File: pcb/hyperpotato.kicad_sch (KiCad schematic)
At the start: 61 parts, among them J1 Conn_01x05, J2 Conn_01x02_Socket, J3 Conn_01x04, J4 Conn_01x04, J5 Conn_01x04, J6 Conn_01x05, K1 SW_Push, K10 SW_Push, K11 SW_Push, K12 SW_Push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

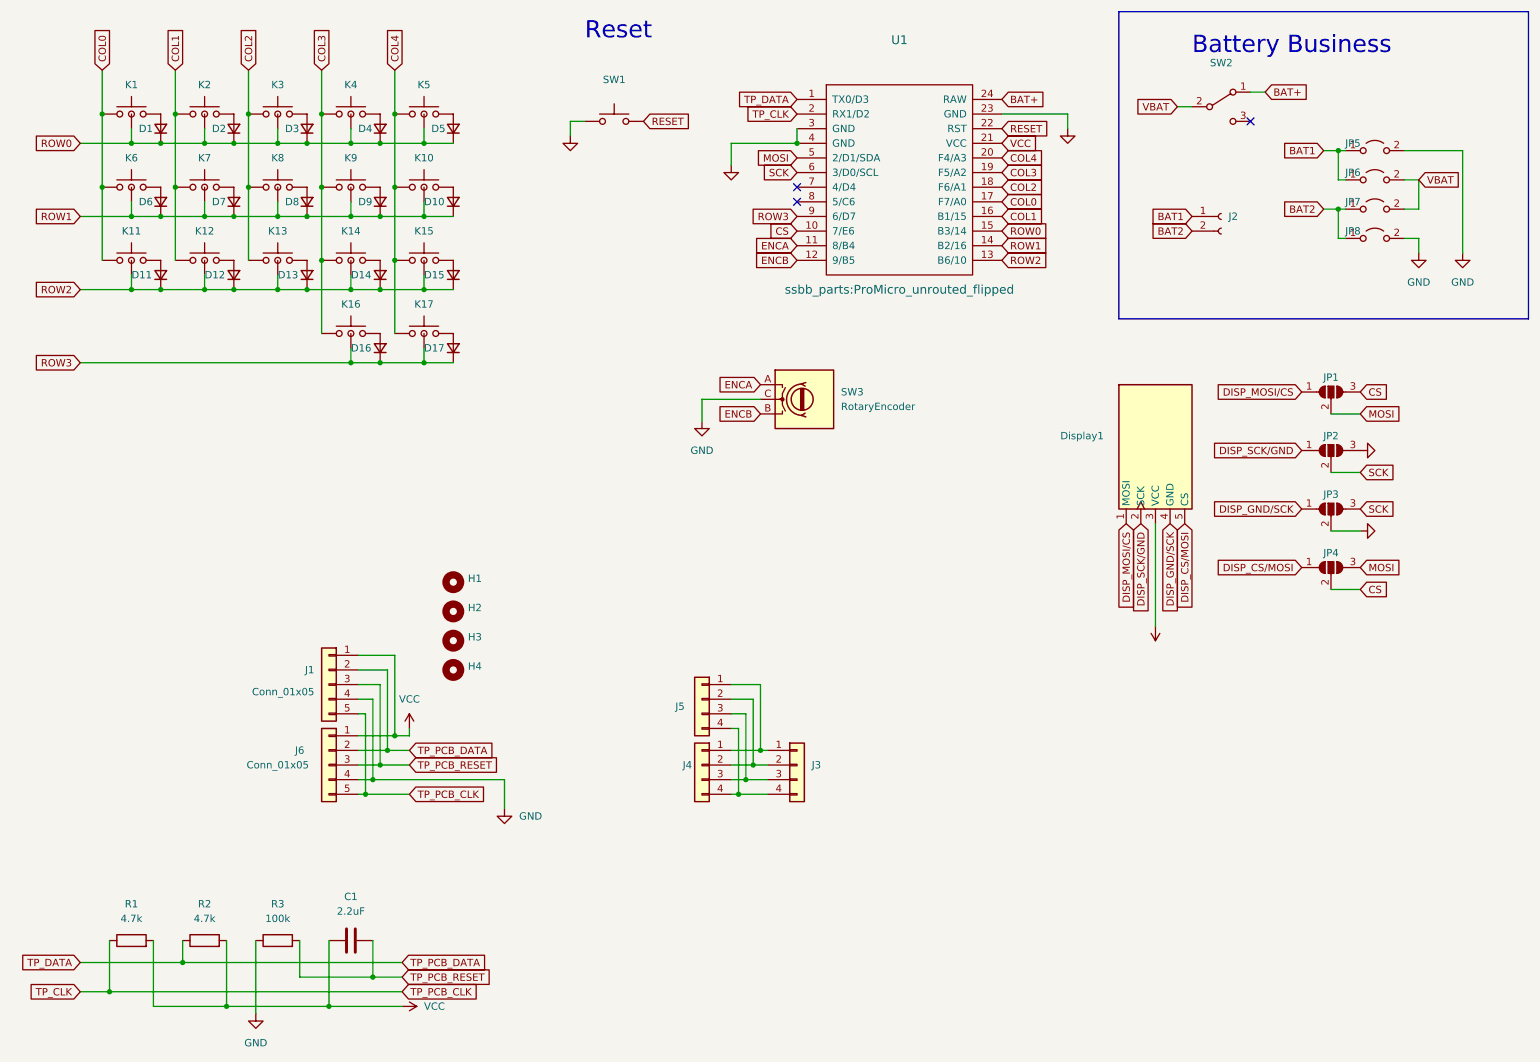
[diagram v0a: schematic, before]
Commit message: Revert "Prepare rev1.3"
This reverts commit 189d012c5a395af6f6aed353e3fd92b88b9e8c79.
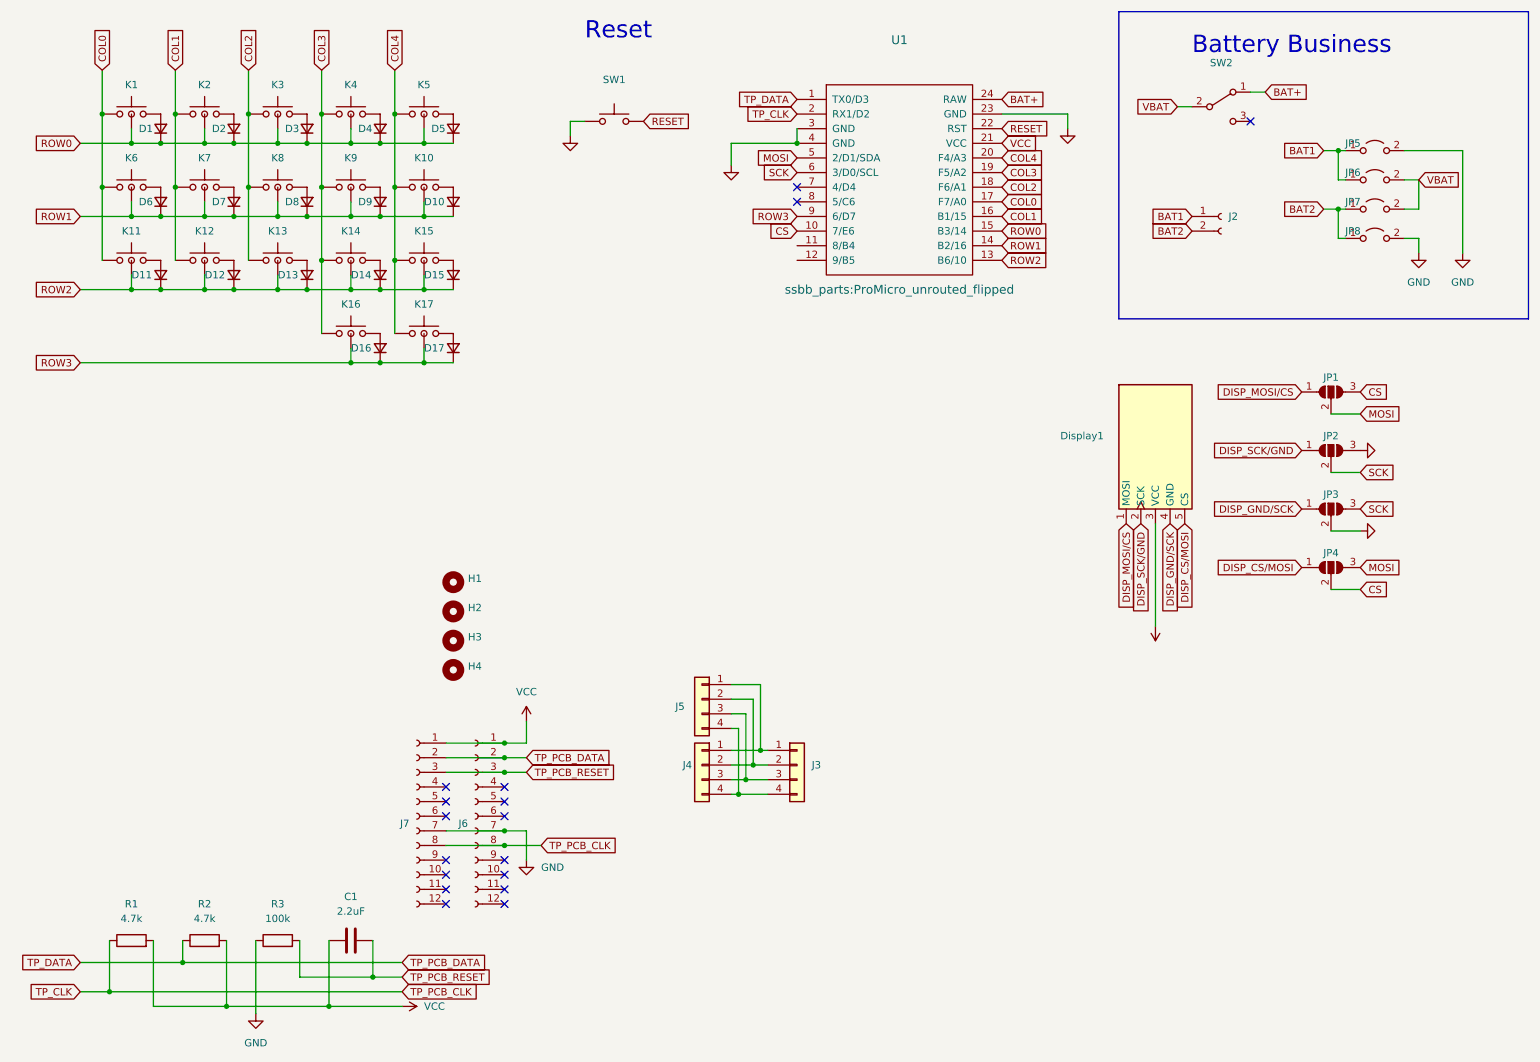
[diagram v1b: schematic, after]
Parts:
- removed J1, J6: Conn_01x05, hyperpotato:Trackpoint_PCB_Connector_alt, symbol Connector_Generic:Conn_01x05
- removed SW3: RotaryEncoder, hyperpotato:RotaryEncoder_Alps_EC12E_Vertical_H20mm, symbol Device:RotaryEncoder
- added J6, J7: Conn_01x12_Socket, hyperpotato:Trackpoint_PCB_Connector, symbol Connector:Conn_01x12_Socket
- K17: footprint hyperpotato:V1_V2_HS_reversible_plated -> hyperpotato:V1_V2_HS_reversible_plated_no_fix_pin
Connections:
- net GND: now also J6.7 (Pin_7), J7.7 (Pin_7)
- net TP_CLK: now also J6.8 (Pin_8), J7.8 (Pin_8)
- net TP_DATA: now also J6.2 (Pin_2), J7.2 (Pin_2)
- net TP_PCB_RESET: now also J6.3 (Pin_3), J7.3 (Pin_3)
- net VCC: now also J6.1 (Pin_1), J7.1 (Pin_1)
- net ENCA: no longer names the net of U1.11 (8/B4)
- net ENCB: no longer names the net of U1.12 (9/B5)
- no-connect marks 3 -> 17

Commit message: Prepare rev1.3
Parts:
- removed J6, J7: Conn_01x12_Socket, hyperpotato:Trackpoint_PCB_Connector, symbol Connector:Conn_01x12_Socket
- added J1, J6: Conn_01x05, hyperpotato:Trackpoint_PCB_Connector_alt, symbol Connector_Generic:Conn_01x05
- added SW3: RotaryEncoder, hyperpotato:RotaryEncoder_Alps_EC12E_Vertical_H20mm, symbol Device:RotaryEncoder
- K17: footprint hyperpotato:V1_V2_HS_reversible_plated_no_fix_pin -> hyperpotato:V1_V2_HS_reversible_plated
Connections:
- net GND: now also J1.4 (Pin_4), J6.4 (Pin_4), SW3.C
- net TP_CLK: now also J1.5 (Pin_5), J6.5 (Pin_5)
- net TP_DATA: now also J1.2 (Pin_2), J6.2 (Pin_2)
- net TP_PCB_RESET: now also J1.3 (Pin_3), J6.3 (Pin_3)
- net VCC: now also J1.1 (Pin_1), J6.1 (Pin_1)
- net ENCA: now reaches U1.11 (8/B4)
- net ENCA: now also SW3.A
- net ENCB: now reaches U1.12 (9/B5)
- net ENCB: now also SW3.B
- no-connect marks 17 -> 3
